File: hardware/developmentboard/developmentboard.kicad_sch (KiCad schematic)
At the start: 1 part

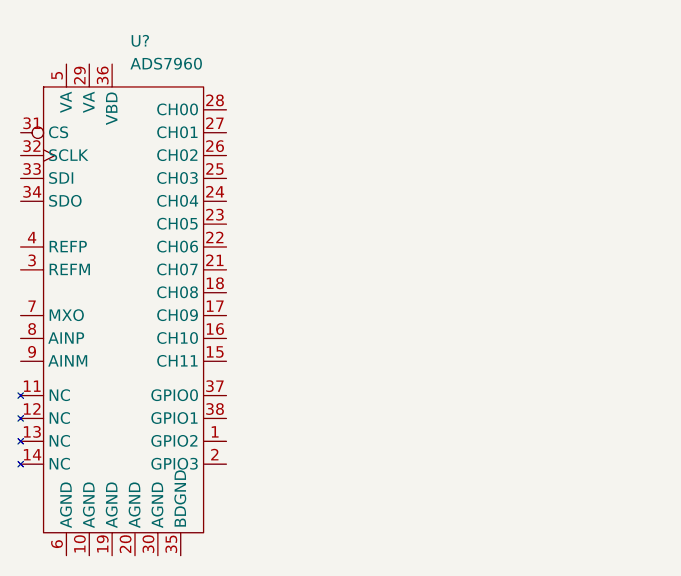
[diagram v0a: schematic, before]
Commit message: made ece library parts relative to project
forgit sym-lib-table
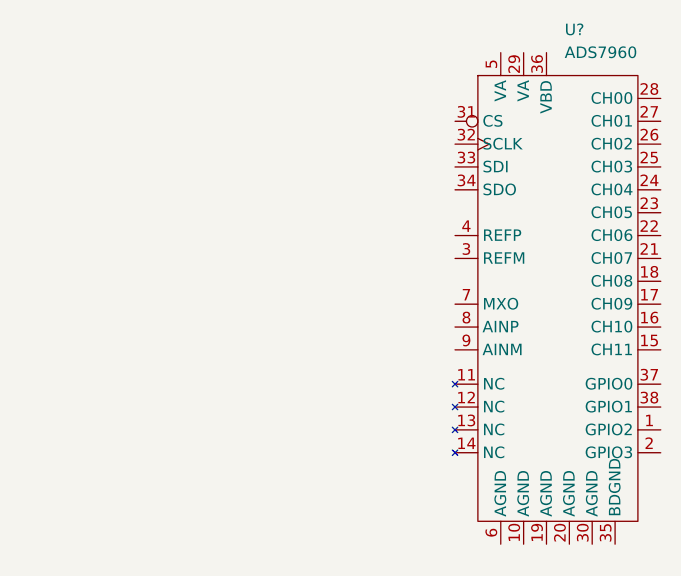
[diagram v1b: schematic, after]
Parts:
- removed U?: ADS7960, Package_SO:TSSOP-38_4.4x9.7mm_P0.5mm, symbol ece_stuff:ADS7960
- added U?: ADS7960, Package_SO:TSSOP-38_4.4x9.7mm_P0.5mm, symbol ece_capstone:ADS7960
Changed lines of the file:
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@@
 (kicad_sch (version 20211123) (generator eeschema)
   (paper "A4")
-  (symbol (lib_id "ece_stuff:ADS7960") (at 83.82 55.88 0) (unit 1)
+  (symbol (lib_id "ece_capstone:ADS7960") (at 132.08 54.61 0) (unit 1)
     (in_bom yes) (on_board yes) (fields_autoplaced)
-    (property "Reference" "U?" (id 0) (at 84.5694 41.91 0)
+    (property "Reference" "U?" (id 0) (at 132.8294 40.64 0)
       (effects (font (size 1.27 1.27)) (justify left))
     )
-    (property "Value" "ADS7960" (id 1) (at 84.5694 44.45 0)
+    (property "Value" "ADS7960" (id 1) (at 132.8294 43.18 0)
       (effects (font (size 1.27 1.27)) (justify left))
     )
-    (property "Footprint" "Package_SO:TSSOP-38_4.4x9.7mm_P0.5mm" (id 2) (at 85.09 69.85 90)
+    (property "Footprint" "Package_SO:TSSOP-38_4.4x9.7mm_P0.5mm" (id 2) (at 133.35 68.58 90)
       (effects (font (size 1 1)) hide)
     )
-    (property "Datasheet" "" (id 3) (at 83.82 55.88 0)
+    (property "Datasheet" "" (id 3) (at 132.08 54.61 0)
       (effects (font (size 1.27 1.27)) hide)
     )
@@
   )
   (symbol_instances
-    (path "/c4729328-3922-4d71-85e2-0c72c3125a59"
+    (path "/eedfbb34-1201-4310-b013-358cf3bc5368"
       (reference "U?") (unit 1) (value "ADS7960") (footprint "Package_SO:TSSOP-38_4.4x9.7mm_P0.5mm")
     )

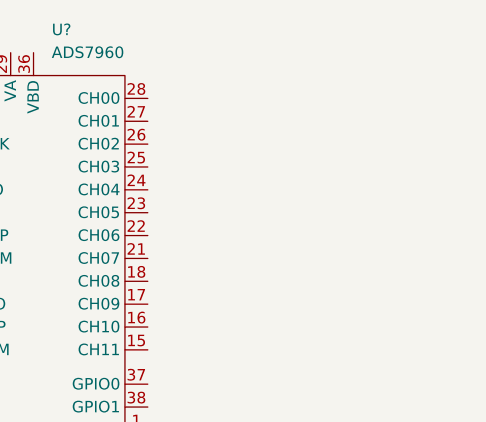
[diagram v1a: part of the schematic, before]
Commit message: added hall-effect sensor
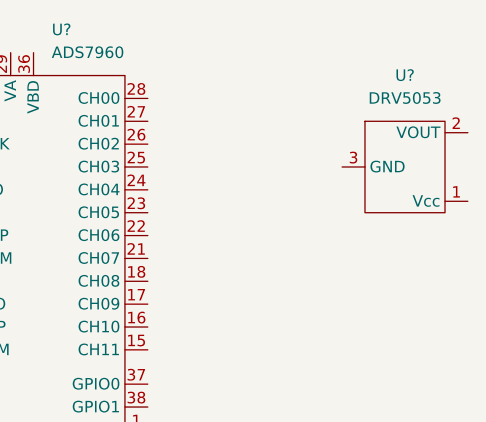
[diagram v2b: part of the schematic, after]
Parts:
- added U?: DRV5053, Package_TO_SOT_SMD:SOT-23, symbol ece_capstone:DRV5053
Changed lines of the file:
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@@
     (pin "9")
+  )
+  (symbol (lib_name "DRV5053_1") (lib_id "ece_capstone:DRV5053") (at 173.99 49.53 0) (unit 1)
+    (in_bom yes) (on_board yes) (fields_autoplaced)
+    (property "Reference" "U?" (id 0) (at 172.085 45.72 0))
+    (property "Value" "DRV5053" (id 1) (at 172.085 48.26 0))
+    (property "Footprint" "Package_TO_SOT_SMD:SOT-23" (id 2) (at 173.99 49.53 0)
+      (effects (font (size 1.27 1.27)) hide)
+    )
+    (property "Datasheet" "" (id 3) (at 173.99 49.53 0)
+      (effects (font (size 1.27 1.27)) hide)
+    )
+    (pin "1")
+    (pin "2")
+    (pin "3")
   )
   (sheet_instances
@@
       (reference "U?") (unit 1) (value "ADS7960") (footprint "Package_SO:TSSOP-38_4.4x9.7mm_P0.5mm")
     )
+    (path "/f988279f-4c4d-4b25-b4fc-c7518a23f719"
+      (reference "U?") (unit 1) (value "DRV5053") (footprint "Package_TO_SOT_SMD:SOT-23")
+    )
   )

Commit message: testing gitignore
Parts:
- gave numbers to parts that had none: 2
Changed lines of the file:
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@@
   (symbol (lib_id "ece_capstone:ADS7960") (at 132.08 54.61 0) (unit 1)
     (in_bom yes) (on_board yes) (fields_autoplaced)
-    (property "Reference" "U?" (id 0) (at 132.8294 40.64 0)
+    (property "Reference" "U1" (id 0) (at 132.8294 40.64 0)
       (effects (font (size 1.27 1.27)) (justify left))
     )
@@
   (symbol (lib_name "DRV5053_1") (lib_id "ece_capstone:DRV5053") (at 173.99 49.53 0) (unit 1)
     (in_bom yes) (on_board yes) (fields_autoplaced)
-    (property "Reference" "U?" (id 0) (at 172.085 45.72 0))
+    (property "Reference" "U2" (id 0) (at 172.085 45.72 0))
     (property "Value" "DRV5053" (id 1) (at 172.085 48.26 0))
     (property "Footprint" "Package_TO_SOT_SMD:SOT-23" (id 2) (at 173.99 49.53 0)
@@
   (symbol_instances
     (path "/eedfbb34-1201-4310-b013-358cf3bc5368"
-      (reference "U?") (unit 1) (value "ADS7960") (footprint "Package_SO:TSSOP-38_4.4x9.7mm_P0.5mm")
+      (reference "U1") (unit 1) (value "ADS7960") (footprint "Package_SO:TSSOP-38_4.4x9.7mm_P0.5mm")
     )
     (path "/f988279f-4c4d-4b25-b4fc-c7518a23f719"
-      (reference "U?") (unit 1) (value "DRV5053") (footprint "Package_TO_SOT_SMD:SOT-23")
+      (reference "U2") (unit 1) (value "DRV5053") (footprint "Package_TO_SOT_SMD:SOT-23")
     )
   )

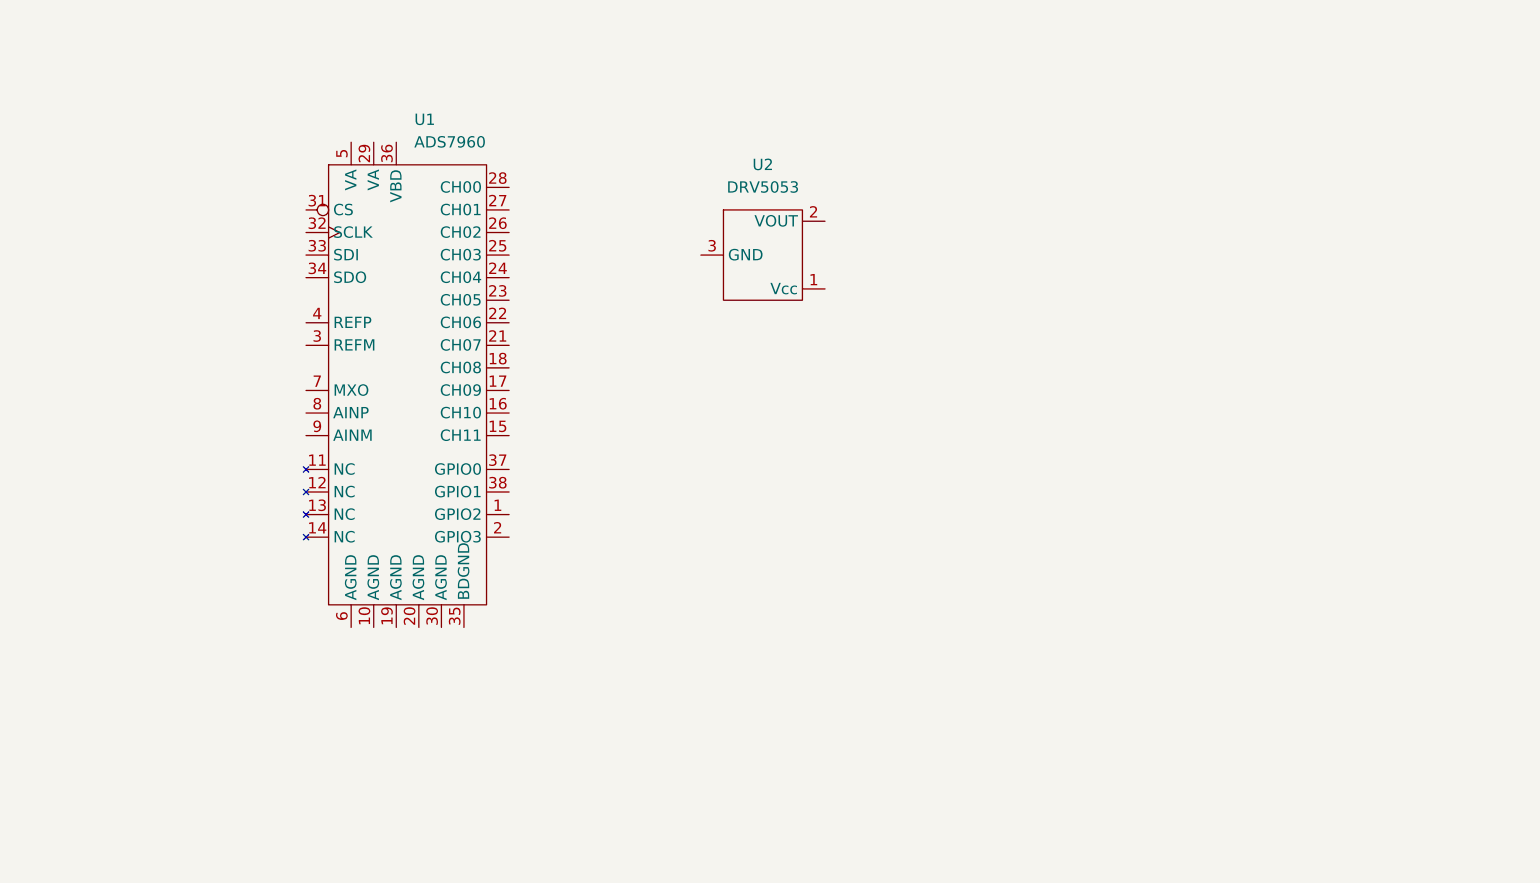
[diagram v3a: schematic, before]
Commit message: Development Board Schematic Changes
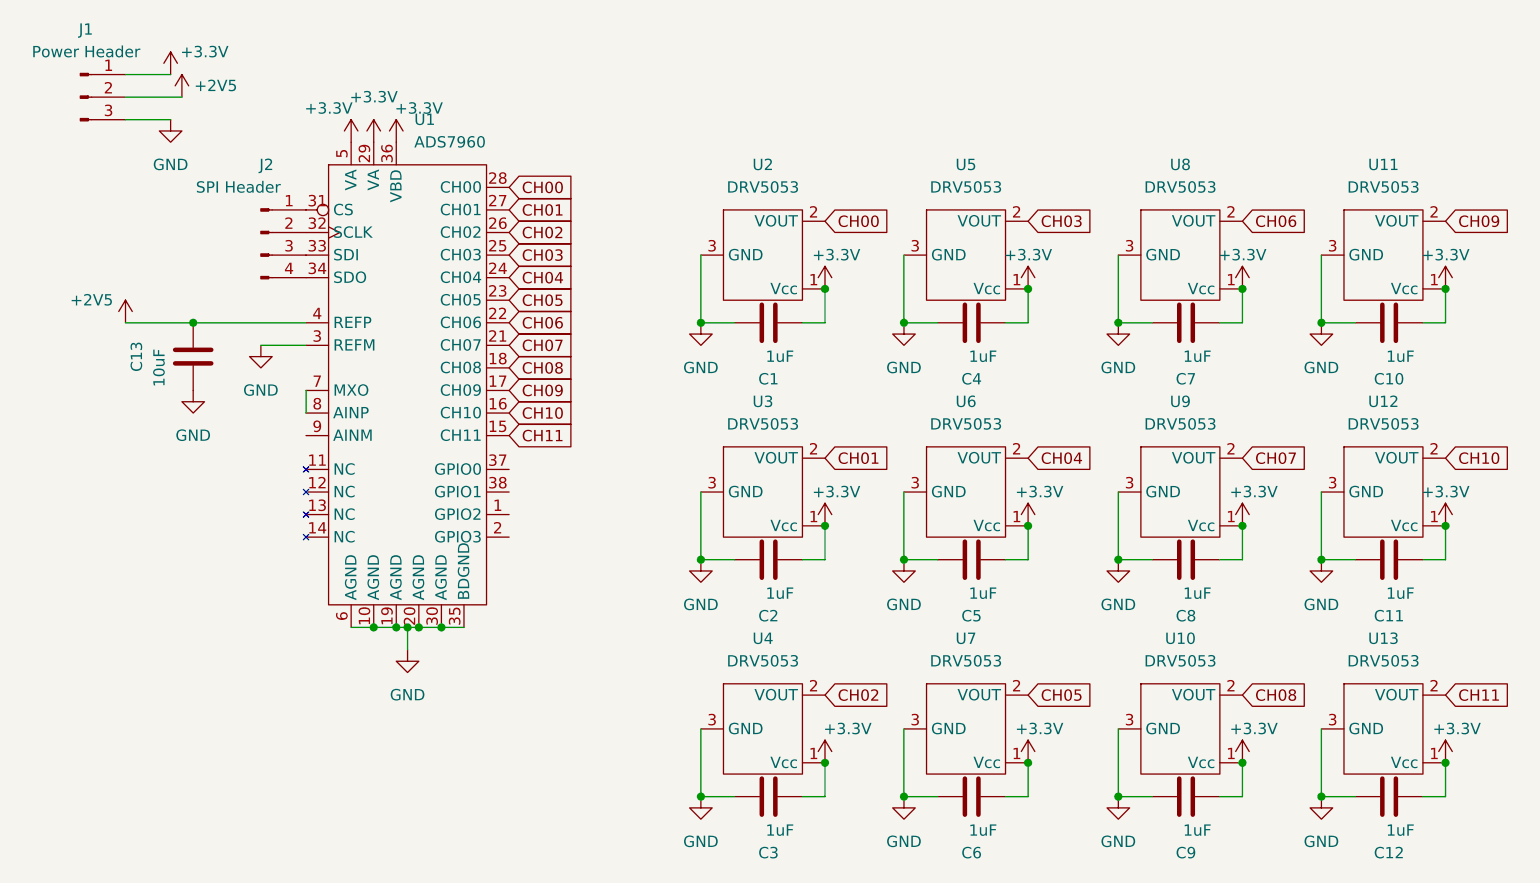
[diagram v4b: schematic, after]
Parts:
- added C1, C10, C11, C12, C2, C3, C4, C5, C6, C7, C8, C9: 1uF, symbol Device:C
- added C13: 10uF, symbol Device:C
- added J1: Power Header, symbol Connector:Conn_01x03_Male
- added J2: SPI Header, symbol Connector:Conn_01x04_Male
- added U10, U11, U12, U13, U3, U4, U5, U6, U7, U8, U9: DRV5053, Package_TO_SOT_SMD:SOT-23, symbol ece_capstone:DRV5053
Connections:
- net GND: now reaches U1.10 (AGND)
- net GND: now also U1.19 (AGND), U1.20 (AGND), U1.3 (REFM), U1.30 (AGND), U1.35 (BDGND), U1.6 (AGND), U2.3 (GND), C1.1, C10.1, C11.1, C12.1, C13.2, C2.1, C3.1, C4.1, C5.1, C6.1, C7.1, C8.1, C9.1, J1.3 (Pin_3), U10.3 (GND), U11.3 (GND), U12.3 (GND), U13.3 (GND), U3.3 (GND), U4.3 (GND), U5.3 (GND), U6.3 (GND), U7.3 (GND), U8.3 (GND), U9.3 (GND)
- net CH11: now reaches U1.15 (CH11)
- net CH11: now also U13.2 (VOUT)
- net CH10: now reaches U1.16 (CH10)
- net CH10: now also U12.2 (VOUT)
- net CH09: now reaches U1.17 (CH09)
- net CH09: now also U11.2 (VOUT)
- net CH08: now reaches U1.18 (CH08)
- net CH08: now also U10.2 (VOUT)
- net CH07: now reaches U1.21 (CH07)
- net CH07: now also U9.2 (VOUT)
- net CH06: now reaches U1.22 (CH06)
- net CH06: now also U8.2 (VOUT)
- net CH05: now reaches U1.23 (CH05)
- net CH05: now also U7.2 (VOUT)
- net CH04: now reaches U1.24 (CH04)
- net CH04: now also U6.2 (VOUT)
- net CH03: now reaches U1.25 (CH03)
- net CH03: now also U5.2 (VOUT)
- net CH02: now reaches U1.26 (CH02)
- net CH02: now also U4.2 (VOUT)
- net CH01: now reaches U1.27 (CH01)
- net CH01: now also U3.2 (VOUT)
- net CH00: now reaches U1.28 (CH00)
- net CH00: now also U2.2 (VOUT)
- net +3.3V: now reaches U1.29 (VA)
- net +3.3V: now also U1.36 (VBD), U1.5 (VA), U2.1 (Vcc), C1.2, C10.2, C11.2, C12.2, C2.2, C3.2, C4.2, C5.2, C6.2, C7.2, C8.2, C9.2, J1.1 (Pin_1), U10.1 (Vcc), U11.1 (Vcc), U12.1 (Vcc), U13.1 (Vcc), U3.1 (Vcc), U4.1 (Vcc), U5.1 (Vcc), U6.1 (Vcc), U7.1 (Vcc), U8.1 (Vcc), U9.1 (Vcc)
- net at U1.31 (CS): now also J2.1 (Pin_1)
- net at U1.32 (SCLK): now also J2.2 (Pin_2)
- net at U1.33 (SDI): now also J2.3 (Pin_3)
- net at U1.34 (SDO): now also J2.4 (Pin_4)
- net +2V5: now reaches U1.4 (REFP)
- net +2V5: now also C13.1, J1.2 (Pin_2)
- net at U1.7 (MXO): now also U1.8 (AINP)

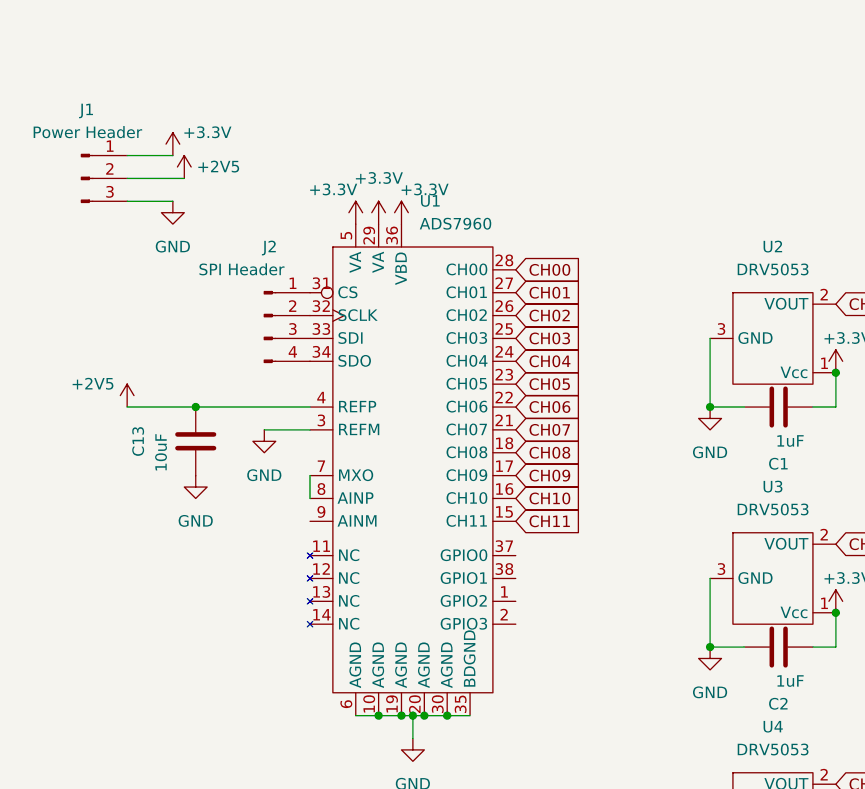
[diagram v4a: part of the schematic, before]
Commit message: Bypassed Va and Vbd to GND with 1uF AINM to GND Breakout pins for ADC pins
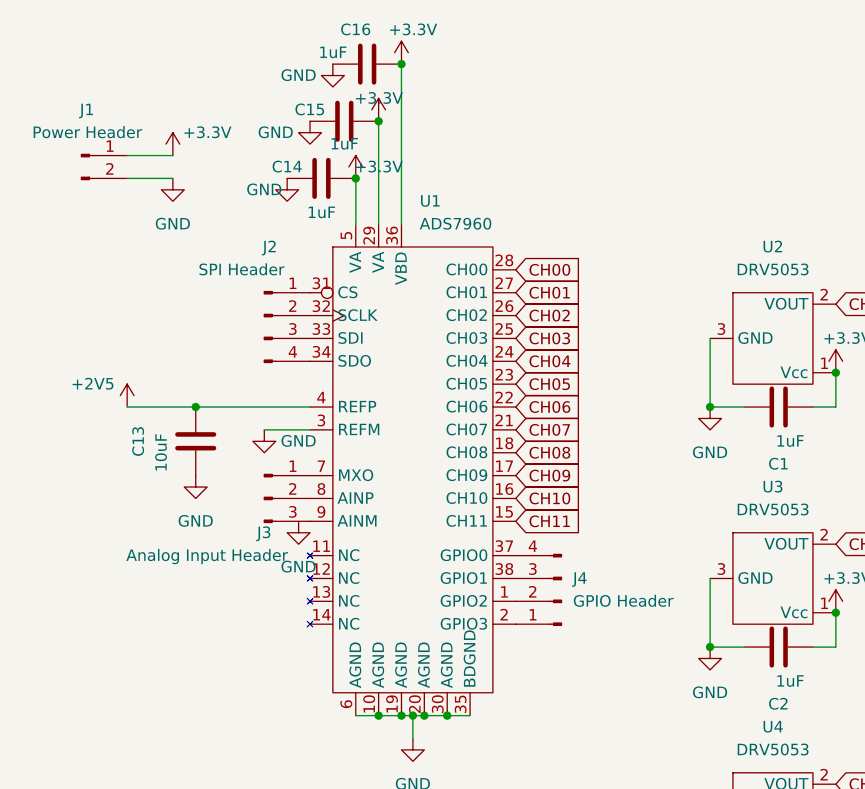
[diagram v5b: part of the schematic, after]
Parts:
- removed J1: Power Header, symbol Connector:Conn_01x03_Male
- added C14, C15, C16: 1uF, symbol Device:C
- added J1: Power Header, symbol Connector:Conn_01x02_Male
- added J3: Analog Input Header, symbol Connector:Conn_01x03_Male
- added J4: GPIO Header, symbol Connector:Conn_01x04_Male
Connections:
- net +3.3V: now also C14.2, C15.2, C16.2, J1.1 (Pin_1)
- net GND: now also C14.1, C15.1, C16.1, J1.2 (Pin_2)
- net at U1.1 (GPIO2): now also J4.2 (Pin_2)
- net at U1.2 (GPIO3): now also J4.1 (Pin_1)
- net at U1.37 (GPIO0): now also J4.4 (Pin_4)
- net at U1.38 (GPIO1): now also J4.3 (Pin_3)
- net at U1.7 (MXO): now also J3.1 (Pin_1); no longer U1.8 (AINP)
- net at U1.9 (AINM): now also J3.3 (Pin_3)
- new net: J3.2 (Pin_2), U1.8 (AINP)
